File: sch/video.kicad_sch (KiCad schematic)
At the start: 0 parts

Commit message: Board layout, addr bus
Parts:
- added J?: (no value), symbol Connector:DB15_Female_HighDensity_MountingHoles
- added U7: STM8S003K3T, Package_QFP:LQFP-32_7x7mm_P0.8mm, symbol MCU_ST_STM8:STM8S003K3T
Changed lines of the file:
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@@
 (kicad_sch (version 20211123) (generator eeschema)
   (paper "A4")
+  (bus_entry (at 51.435 91.44) (size 2.54 2.54)
+    (stroke (width 0) (type default) (color 0 0 0 0))
+  )
+  (hierarchical_label "D[0..7]" (shape bidirectional) (at 67.31 66.675 180)
+    (effects (font (size 1.27 1.27)) (justify right))
+  )
+  (hierarchical_label "~{VID_CS}" (shape input) (at 67.31 71.12 180)
+    (effects (font (size 1.27 1.27)) (justify right))
+  )
+  (hierarchical_label "A[0..23]" (shape input) (at 67.31 60.96 180)
+    (effects (font (size 1.27 1.27)) (justify right))
+  )
+  (symbol (lib_id "Connector:DB15_Female_HighDensity_MountingHoles") (at 180.975 73.66 0) (unit 1)
+    (in_bom yes) (on_board yes) (fields_autoplaced)
+    (property "Reference" "J?" (id 0) (at 180.975 50.8 0))
+    (property "Value" "" (id 1) (at 180.975 53.34 0))
+    (property "Footprint" "" (id 2) (at 156.845 63.5 0)
+      (effects (font (size 1.27 1.27)) hide)
+    )
+    (property "Datasheet" " ~" (id 3) (at 156.845 63.5 0)
+      (effects (font (size 1.27 1.27)) hide)
+    )
+    (pin "0")
+    (pin "1")
+    (pin "10")
+    (pin "11")
+    (pin "12")
+    (pin "13")
+    (pin "14")
+    (pin "15")
+    (pin "2")
+    (pin "3")
+    (pin "4")
+    (pin "5")
+    (pin "6")
+    (pin "7")
+    (pin "8")
+    (pin "9")
+  )
+  (symbol (lib_id "MCU_ST_STM8:STM8S003K3T") (at 133.985 92.075 0) (unit 1)
+    (in_bom yes) (on_board yes) (fields_autoplaced)
+    (property "Reference" "U7" (id 0) (at 136.0044 54.61 0)
+      (effects (font (size 1.27 1.27)) (justify left))
+    )
+    (property "Value" "STM8S003K3T" (id 1) (at 136.0044 57.15 0)
+      (effects (font (size 1.27 1.27)) (justify left))
+    )
+    (property "Footprint" "Package_QFP:LQFP-32_7x7mm_P0.8mm" (id 2) (at 135.255 53.975 0)
+      (effects (font (size 1.27 1.27)) (justify left) hide)
+    )
+    (property "Datasheet" "http://www.st.com/st-web-ui/static/active/en/resource/technical/document/datasheet/DM00024550.pdf" (id 3) (at 133.985 92.075 0)
+      (effects (font (size 1.27 1.27)) hide)
+    )
+    (pin "1")
+    (pin "10")
+    (pin "11")
+    (pin "12")
+    (pin "13")
+    (pin "14")
+    (pin "15")
+    (pin "16")
+    (pin "17")
+    (pin "18")
+    (pin "19")
+    (pin "2")
+    (pin "20")
+    (pin "21")
+    (pin "22")
+    (pin "23")
+    (pin "24")
+    (pin "25")
+    (pin "26")
+    (pin "27")
+    (pin "28")
+    (pin "29")
+    (pin "3")
+    (pin "30")
+    (pin "31")
+    (pin "32")
+    (pin "4")
+    (pin "5")
+    (pin "6")
+    (pin "7")
+    (pin "8")
+    (pin "9")
+  )
 )

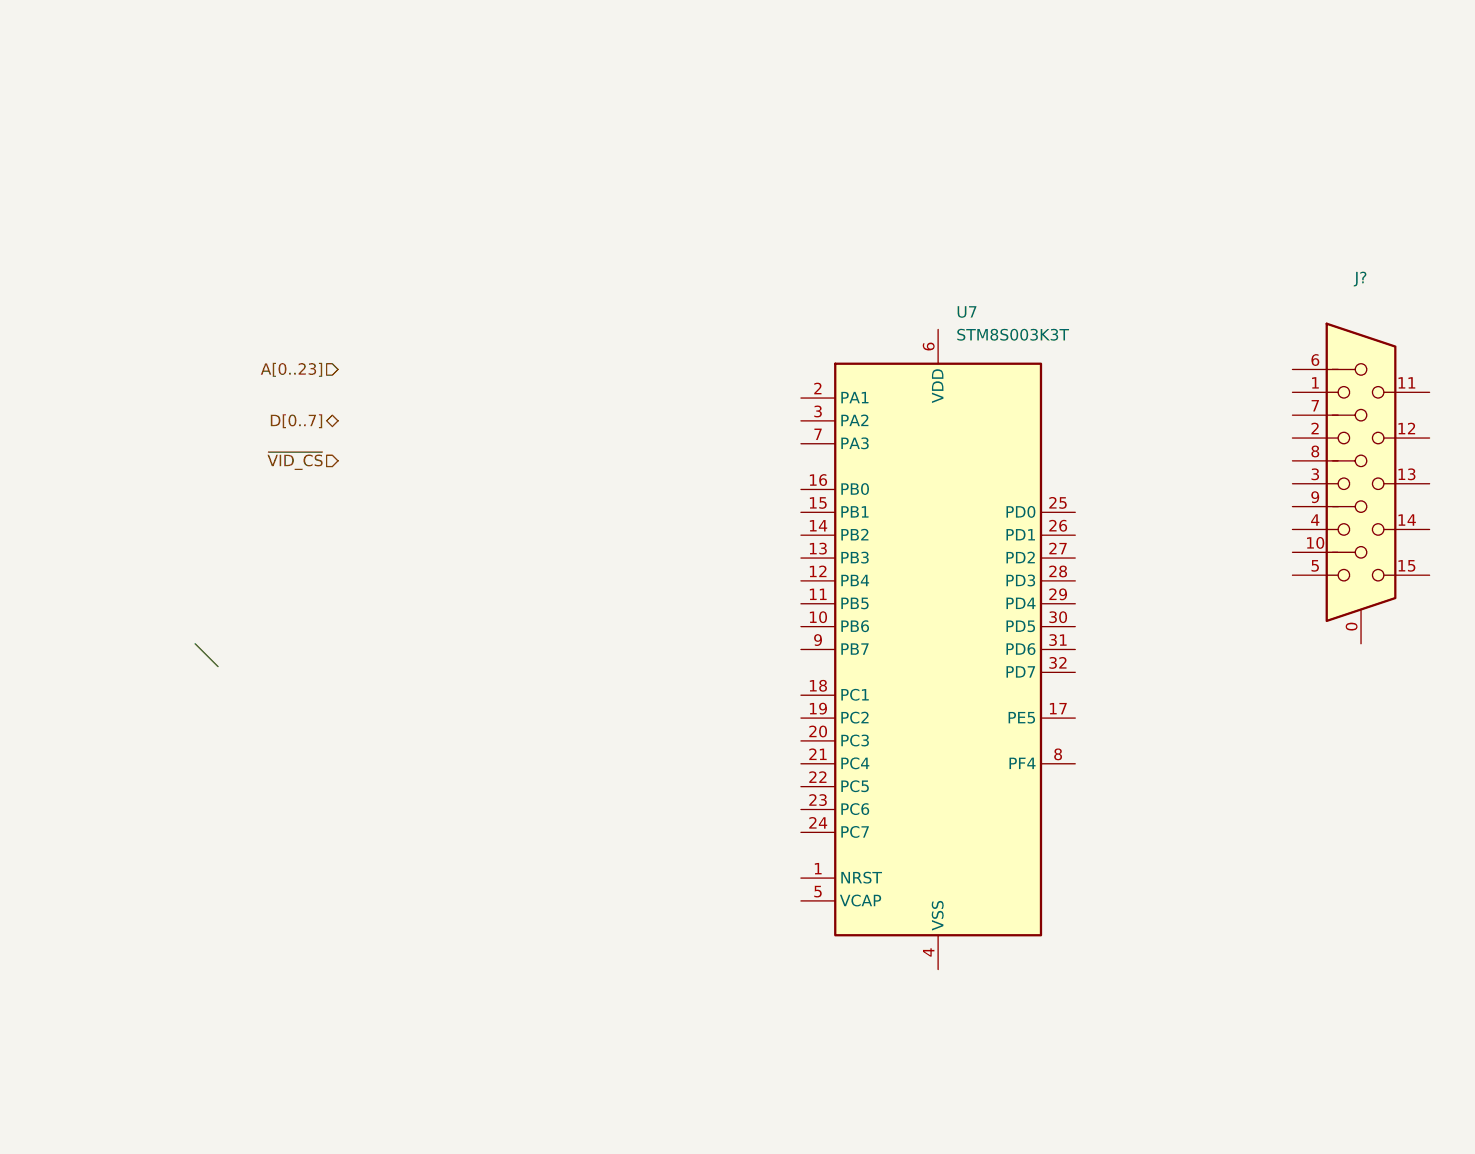
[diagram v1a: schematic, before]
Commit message: More routing, USB iface
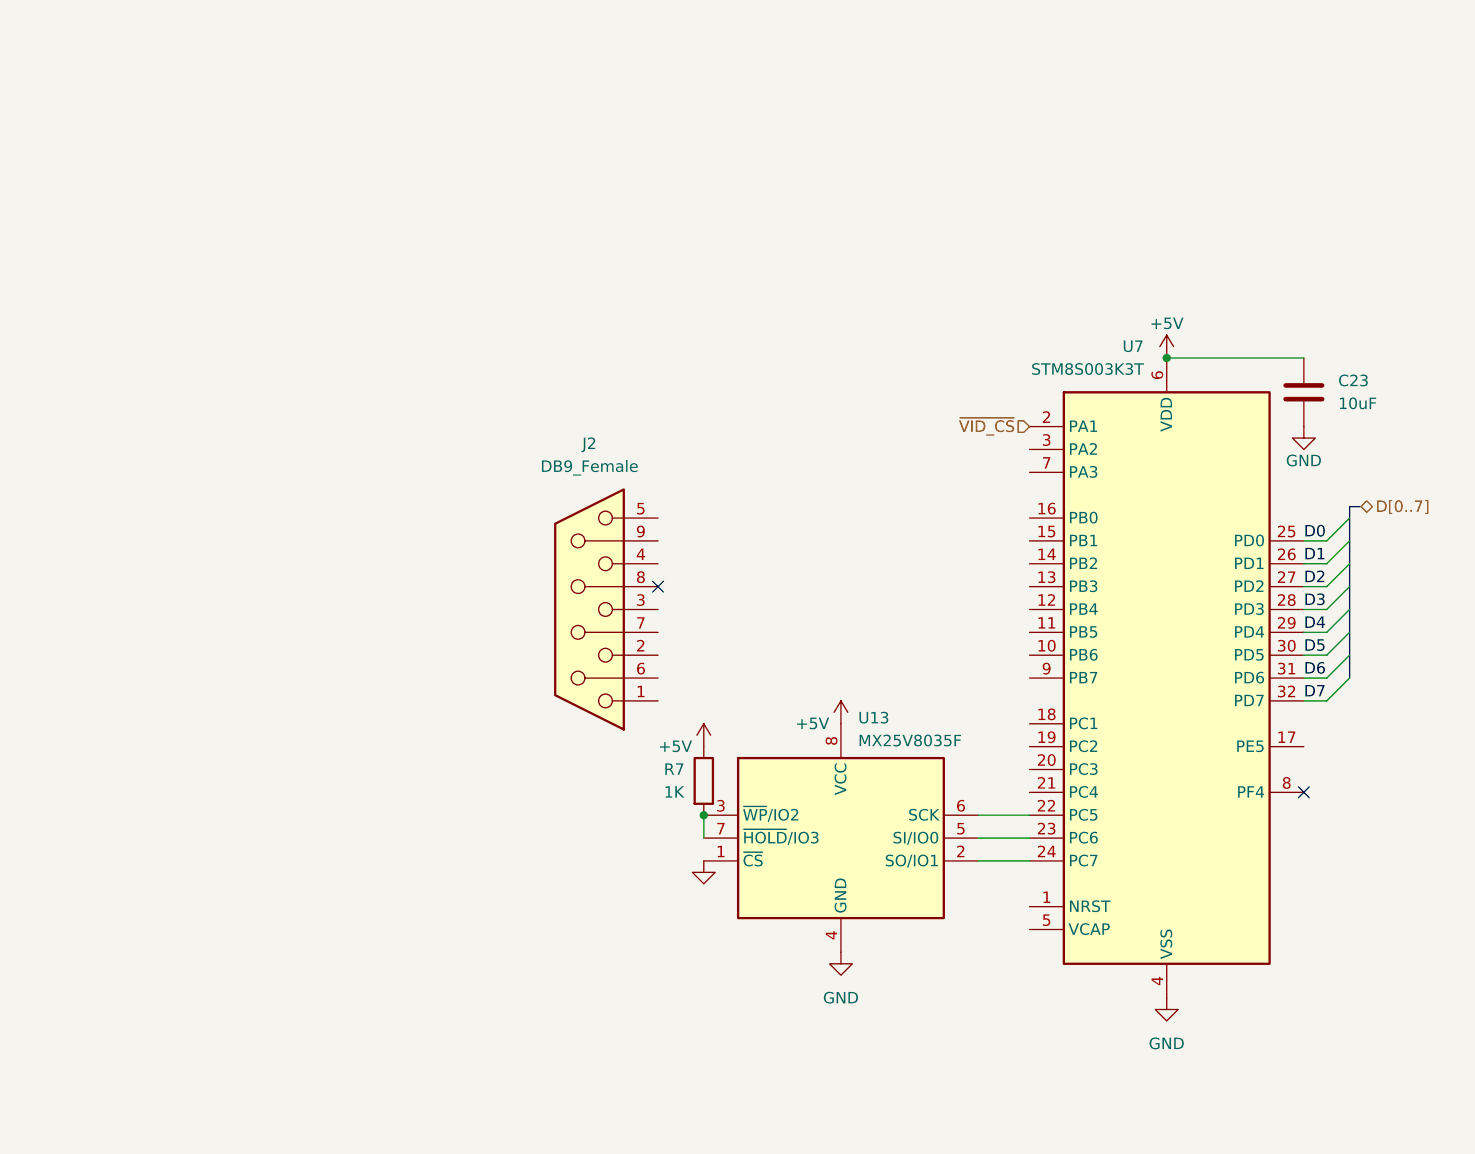
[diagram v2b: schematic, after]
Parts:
- removed J?: (no value), symbol Connector:DB15_Female_HighDensity_MountingHoles
- added C23: 10uF, Capacitor_SMD:C_1206_3216Metric, symbol Device:C
- added J2: DB9_Female, Connector_Dsub:DSUB-9_Female_Horizontal_P2.77x2.84mm_EdgePinOffset9.90mm_Housed_MountingHolesOffset11.32mm, symbol Connector:DB9_Female
- added R7: 1K, Resistor_SMD:R_0603_1608Metric, symbol Device:R
- added U13: MX25V8035F, Package_SO:SOP-8_3.9x4.9mm_P1.27mm, symbol Custom:MX25V8035F
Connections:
- net ~{VID_CS}: now also U7.2 (PA1)
- net at U7.22 (PC5): now also U13.6 (SCK)
- net at U7.23 (PC6): now also U13.5 (SI/IO0)
- net at U7.24 (PC7): now also U13.2 (SO/IO1)
- net D0: now reaches U7.25 (PD0)
- net D1: now reaches U7.26 (PD1)
- net D2: now reaches U7.27 (PD2)
- net D3: now reaches U7.28 (PD3)
- net D4: now reaches U7.29 (PD4)
- net D5: now reaches U7.30 (PD5)
- net D6: now reaches U7.31 (PD6)
- net D7: now reaches U7.32 (PD7)
- net GND: now reaches U7.4 (VSS)
- net GND: now also C23.2, U13.1 (~{CS}), U13.4 (GND)
- net +5V: now reaches U7.6 (VDD)
- net +5V: now also C23.1, R7.1, U13.8 (VCC)
- new net: R7.2, U13.3 (~{WP}/IO2), U13.7 (~{HOLD}/IO3)
- no-connect marks 0 -> 2
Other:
- moved on the sheet: U7

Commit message: Serial interface
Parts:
- removed J2: DB9_Female, Connector_Dsub:DSUB-9_Female_Horizontal_P2.77x2.84mm_EdgePinOffset9.90mm_Housed_MountingHolesOffset11.32mm, symbol Connector:DB9_Female
- removed R7: 1K, Resistor_SMD:R_0603_1608Metric, symbol Device:R
- removed U13: MX25V8035F, Package_SO:SOP-8_3.9x4.9mm_P1.27mm, symbol Custom:MX25V8035F
- removed U7: STM8S003K3T, Package_QFP:LQFP-32_7x7mm_P0.8mm, symbol MCU_ST_STM8:STM8S003K3T
- added J2: (no value), symbol Connector:DB15_Female
- added VIDEO1: (no value), symbol MCU_ST_STM32F3:STM32F301C6Tx
- C23: footprint Capacitor_SMD:C_1206_3216Metric -> (none)
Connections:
- net +5V: now also VIDEO1.1 (VBAT), VIDEO1.24 (VDD), VIDEO1.36 (VDD), VIDEO1.48 (VDD), VIDEO1.9 (VDDA)
- net D0: now also VIDEO1.18 (PB0)
- net D1: now also VIDEO1.19 (PB1)
- net D2: now also VIDEO1.20 (PB2)
- net D3: now also VIDEO1.39 (PB3)
- net D4: now also VIDEO1.40 (PB4)
- net D5: now also VIDEO1.41 (PB5)
- net D6: now also VIDEO1.42 (PB6)
- net D7: now also VIDEO1.43 (PB7)
- net GND: now also VIDEO1.23 (VSS), VIDEO1.35 (VSS), VIDEO1.47 (VSS), VIDEO1.8 (VSSA)
- net ~{VID_CS}: now also VIDEO1.2 (PC13)
- no-connect marks 2 -> 0
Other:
- company: (none) -> zrthxn
- title: (none) -> 8puter
- moved on the sheet: C23

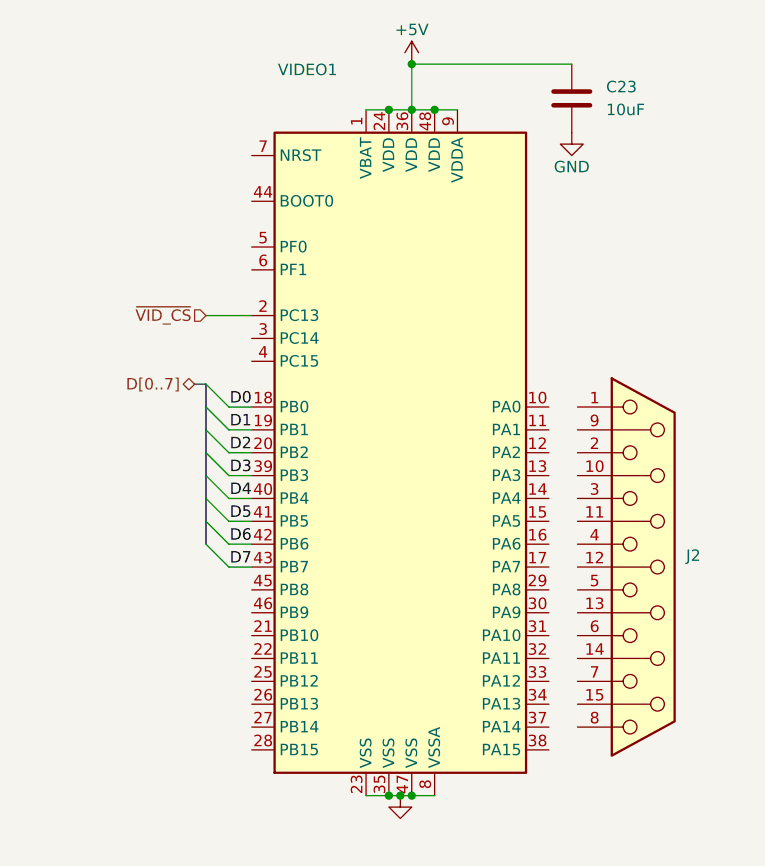
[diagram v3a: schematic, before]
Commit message: Serial, debug and prph headers
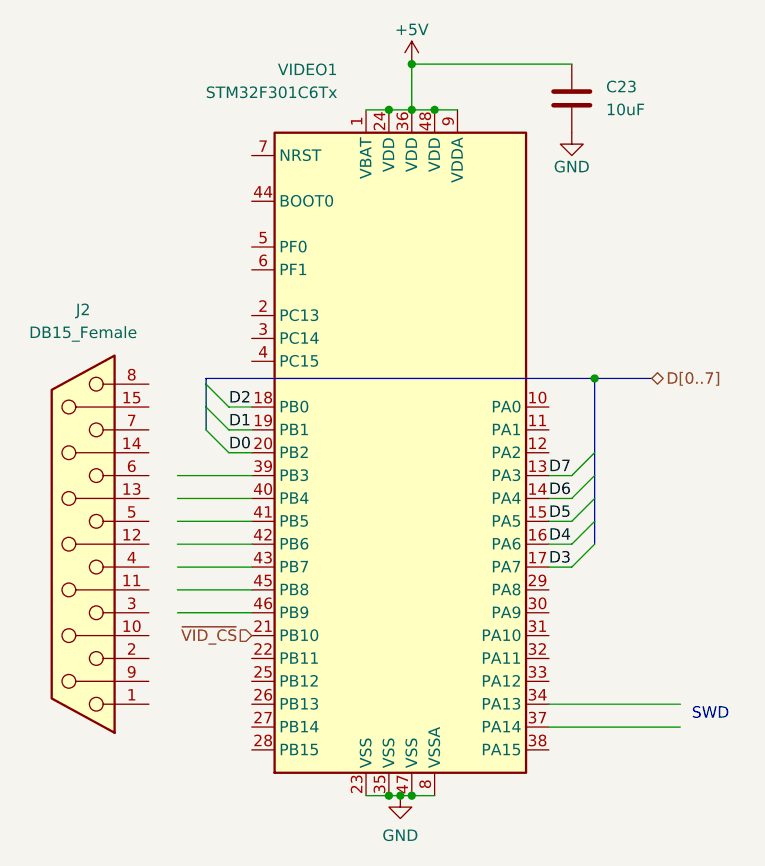
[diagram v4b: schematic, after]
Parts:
- C23: footprint (none) -> Capacitor_SMD:C_0805_2012Metric
- J2: value (none) -> DB15_Female; footprint (none) -> Connector_Dsub:DSUB-15-HD_Female_Horizontal_P2.29x1.98mm_EdgePinOffset3.03mm_Housed_MountingHolesOffset4.94mm
- VIDEO1: value (none) -> STM32F301C6Tx; footprint (none) -> Package_QFP:LQFP-48_7x7mm_P0.5mm
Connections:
- net D0: now also VIDEO1.20 (PB2); no longer VIDEO1.18 (PB0)
- net D2: now also VIDEO1.18 (PB0); no longer VIDEO1.20 (PB2)
- net D3: now also VIDEO1.17 (PA7); no longer VIDEO1.39 (PB3)
- net D4: now also VIDEO1.16 (PA6); no longer VIDEO1.40 (PB4)
- net D5: now also VIDEO1.15 (PA5); no longer VIDEO1.41 (PB5)
- net D6: now also VIDEO1.14 (PA4); no longer VIDEO1.42 (PB6)
- net D7: now also VIDEO1.13 (PA3); no longer VIDEO1.43 (PB7)
- net ~{VID_CS}: now also VIDEO1.21 (PB10); no longer VIDEO1.2 (PC13)
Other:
- note added: "SWD"
- moved on the sheet: J2

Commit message: First completed routing
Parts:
- added SWD_H1: (no value), symbol Connector_Generic:Conn_01x04
- C23: value 10uF -> (none)
- renumbered J2 to VGA1
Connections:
- net GND: now also VGA1.10 (P10), VGA1.5, VGA1.6, VGA1.7, VGA1.8, SWD_H1.4 (Pin_4)
- net COLOR: now reaches VGA1.1
- net COLOR: now also VGA1.2, VGA1.3, VIDEO1.41 (PB5)
- net HSYNC: now reaches VGA1.13 (P13)
- net HSYNC: now also VIDEO1.29 (PA8)
- net VSYNC: now reaches VGA1.14 (P14)
- net VSYNC: now also VIDEO1.11 (PA1)
- net CLOCK: now reaches VIDEO1.22 (PB11)
- net at VIDEO1.34 (PA13): now also SWD_H1.2 (Pin_2)
- net at VIDEO1.37 (PA14): now also SWD_H1.3 (Pin_3)
- net ~{RESET}: now reaches VIDEO1.7 (NRST)
- net +5V renamed +3V0
- net +3V0: now also SWD_H1.1 (Pin_1)
- no-connect marks 0 -> 2
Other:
- note removed: "SWD"
- moved on the sheet: VGA1

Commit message: Gerber Plots
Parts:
- C23: value (none) -> 100nF
- SWD_H1: value (none) -> Conn_01x04; footprint (none) -> Connector_PinHeader_2.00mm:PinHeader_1x04_P2.00mm_Vertical
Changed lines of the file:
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@@
       (effects (font (size 1.27 1.27)) (justify left))
     )
-    (property "Value" "" (id 1) (at 177.8 132.7149 0)
+    (property "Value" "Conn_01x04" (id 1) (at 177.8 132.7149 0)
       (effects (font (size 1.27 1.27)) (justify left))
     )
-    (property "Footprint" "" (id 2) (at 175.26 130.175 0)
+    (property "Footprint" "Connector_PinHeader_2.00mm:PinHeader_1x04_P2.00mm_Vertical" (id 2) (at 175.26 130.175 0)
       (effects (font (size 1.27 1.27)) hide)
     )
@@
       (effects (font (size 1.27 1.27)) (justify left))
     )
-    (property "Value" "" (id 1) (at 163.195 64.135 0)
+    (property "Value" "100nF" (id 1) (at 163.195 64.135 0)
       (effects (font (size 1.27 1.27)) (justify left))
     )

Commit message: some docs
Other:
- note added: "Video Controller"
- note added: "Video will be generated using a microcontroller which is fast enough to generate the VGA timing signals. CPU will send a single byte to the MCU which can be be a char code or index of glyph, and the MCU just generates the video signal. This setup is limited in generating graphics but it avoids having to keep a large framebuffer."
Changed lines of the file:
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@@
     (stroke (width 0) (type default) (color 0 0 0 0))
+  )
+  (text "Video will be generated using a \nmicrocontroller which is fast enough to \ngenerate the VGA timing signals.\n\nCPU will send a single byte to the MCU which can\nbe be a char code or index of glyph, and the MCU\njust generates the video signal.\n\nThis setup is limited in generating graphics but\nit avoids having to keep a large framebuffer."
+    (at 31.75 52.705 0)
+    (effects (font (size 1.27 1.27)) (justify left bottom))
+  )
+  (text "Video Controller" (at 31.75 25.4 0)
+    (effects (font (size 2 2) (thickness 0.4) bold) (justify left bottom))
   )
   (label "HSYNC" (at 109.22 92.075 180)
